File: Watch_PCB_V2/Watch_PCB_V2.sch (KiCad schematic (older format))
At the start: 14 parts

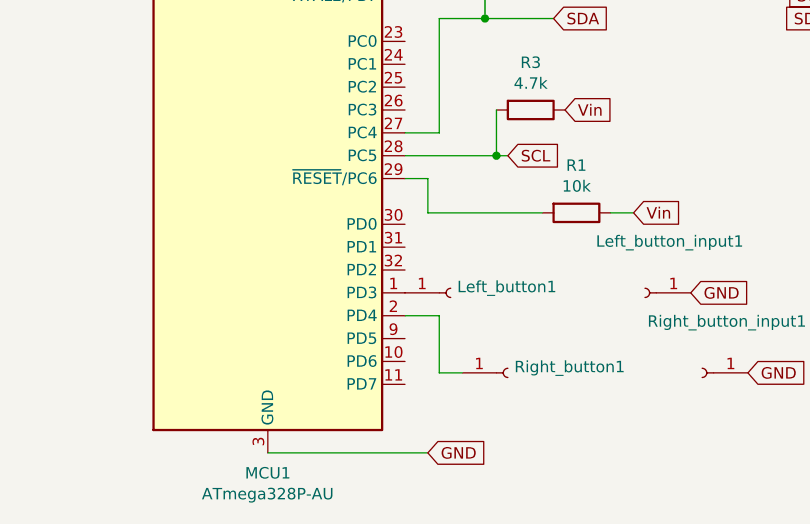
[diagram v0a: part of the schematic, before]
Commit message: PCB: deep sleep interrupt now attached left button input
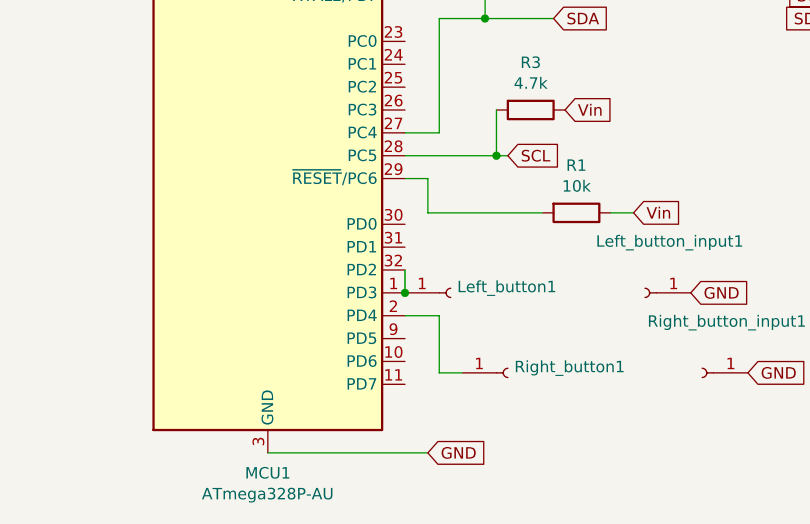
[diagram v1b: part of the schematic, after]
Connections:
- net at Left_button1.1 (Pin_1), MCU1.1 (PD3): now also MCU1.32 (PD2)
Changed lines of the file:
@@
 	-1   0    0    1
 $EndComp
+Wire Wire Line
+	4750 3450 4750 3550
+Connection ~ 4750 3550
 $EndSCHEMATC
